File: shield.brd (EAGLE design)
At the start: 25.6 x 28 mm, 12 parts

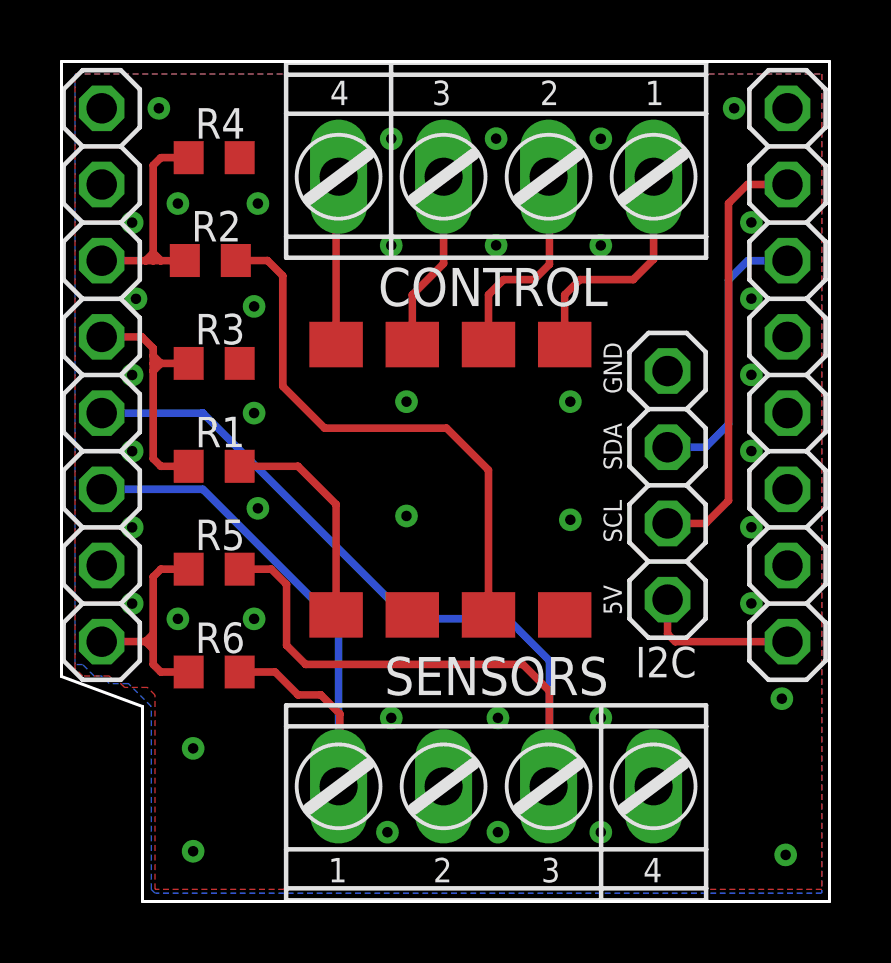
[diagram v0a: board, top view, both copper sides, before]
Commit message: Tweak layout and add lables
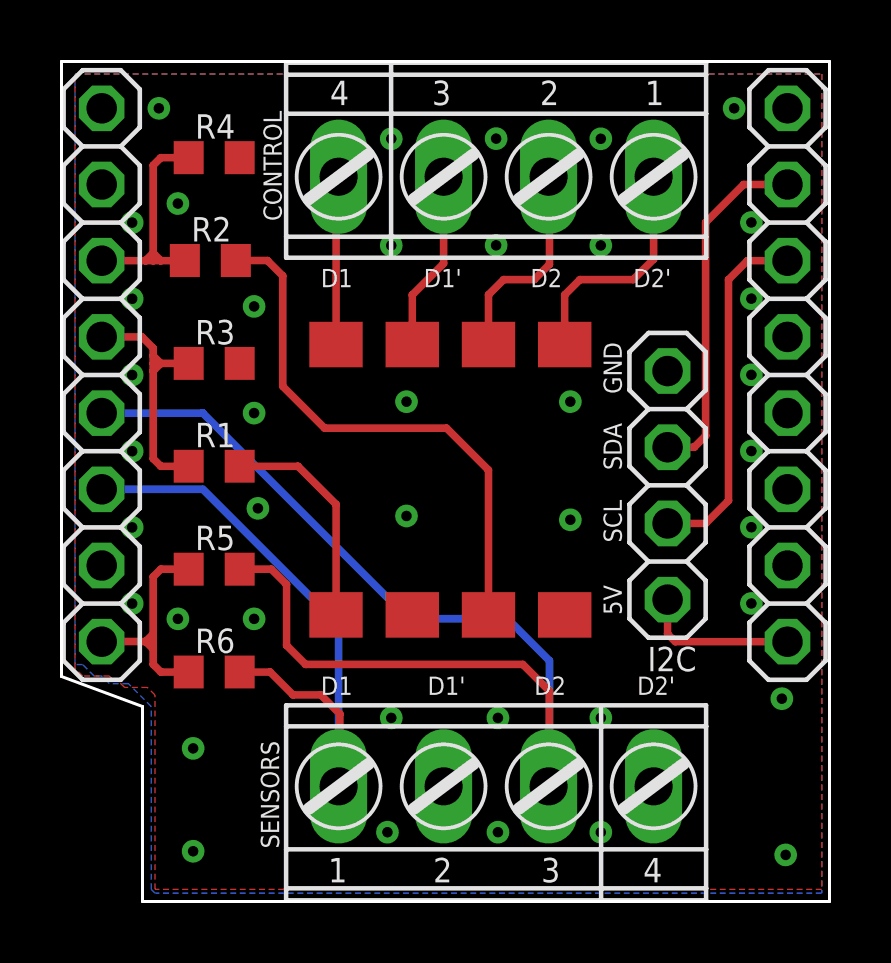
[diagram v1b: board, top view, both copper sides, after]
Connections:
- net D1: now also WEMOS_R.3; no longer WEMOS_R.2
- net D2: now also WEMOS_R.2; no longer WEMOS_R.3
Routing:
- net D1: track 14.5 -> 11.9 mm
- net D2: track 9.40 -> 11.8 mm
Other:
- board text added: "D1"
- board text added: "D1'"
- board text added: "D2"
- board text added: "D2'"

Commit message: tweak silkscreen and add some missing files
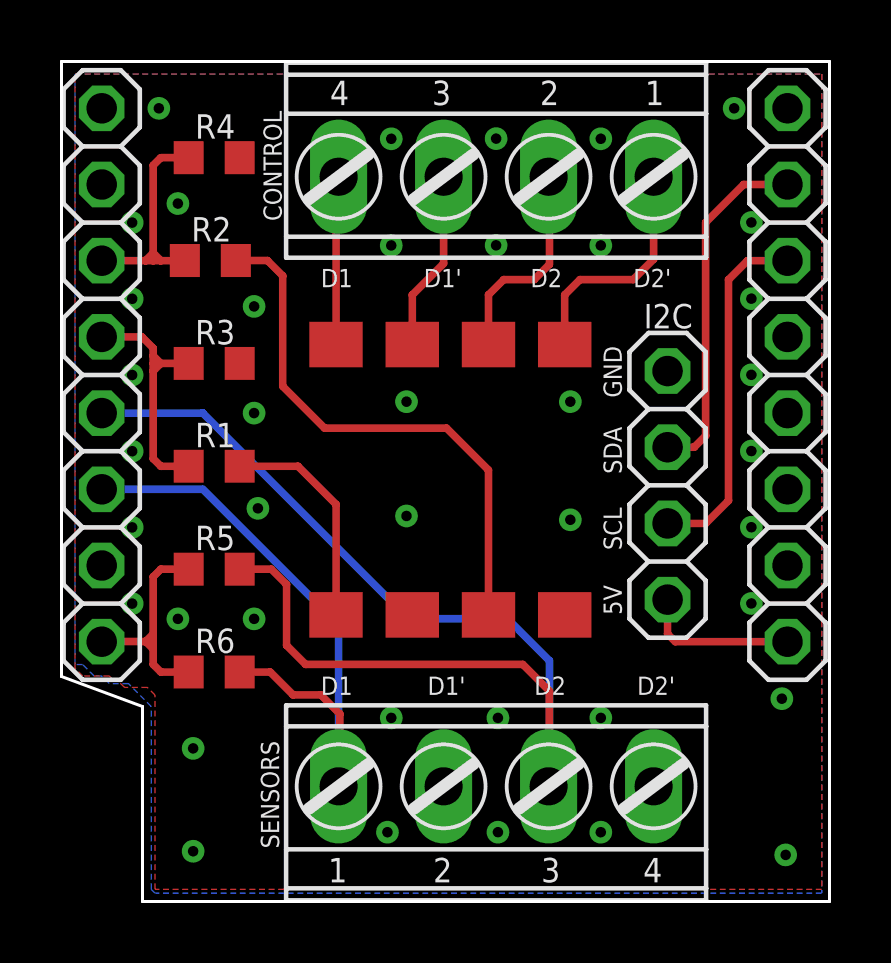
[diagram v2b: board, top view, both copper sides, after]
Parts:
- CONTROL, SENSORS: device con-ptr500:AK550/4 -> shield:AK550/4
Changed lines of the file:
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@@
 <grid distance="5" unitdist="mil" unit="mil" style="lines" multiple="1" display="yes" altdistance="5" altunitdist="mil" altunit="mil"/>
 <layers>
-<layer number="1" name="Top" color="4" fill="1" visible="yes" active="yes"/>
-<layer number="16" name="Bottom" color="1" fill="1" visible="no" active="yes"/>
+<layer number="1" name="Top" color="4" fill="1" visible="no" active="yes"/>
+<layer number="16" name="Bottom" color="1" fill="1" visible="yes" active="yes"/>
 <layer number="17" name="Pads" color="2" fill="1" visible="yes" active="yes"/>
 <layer number="18" name="Vias" color="2" fill="1" visible="yes" active="yes"/>
 <layer number="19" name="Unrouted" color="6" fill="1" visible="yes" active="yes"/>
 <layer number="20" name="Dimension" color="24" fill="1" visible="yes" active="yes"/>
-<layer number="21" name="tPlace" color="7" fill="1" visible="yes" active="yes"/>
-<layer number="22" name="bPlace" color="7" fill="1" visible="no" active="yes"/>
-<layer number="23" name="tOrigins" color="15" fill="1" visible="yes" active="yes"/>
-<layer number="24" name="bOrigins" color="15" fill="1" visible="no" active="yes"/>
-<layer number="25" name="tNames" color="7" fill="1" visible="yes" active="yes"/>
-<layer number="26" name="bNames" color="7" fill="1" visible="no" active="yes"/>
+<layer number="21" name="tPlace" color="7" fill="1" visible="no" active="yes"/>
+<layer number="22" name="bPlace" color="7" fill="1" visible="yes" active="yes"/>
+<layer number="23" name="tOrigins" color="15" fill="1" visible="no" active="yes"/>
+<layer number="24" name="bOrigins" color="15" fill="1" visible="yes" active="yes"/>
+<layer number="25" name="tNames" color="7" fill="1" visible="no" active="yes"/>
+<layer number="26" name="bNames" color="7" fill="1" visible="yes" active="yes"/>
 <layer number="27" name="tValues" color="7" fill="1" visible="no" active="yes"/>
 <layer number="28" name="bValues" color="7" fill="1" visible="no" active="yes"/>
@@
 <layer number="37" name="tTest" color="7" fill="1" visible="no" active="yes"/>
 <layer number="38" name="bTest" color="7" fill="1" visible="no" active="yes"/>
-<layer number="39" name="tKeepout" color="4" fill="11" visible="yes" active="yes"/>
-<layer number="40" name="bKeepout" color="1" fill="11" visible="no" active="yes"/>
-<layer number="41" name="tRestrict" color="4" fill="10" visible="yes" active="yes"/>
-<layer number="42" name="bRestrict" color="1" fill="10" visible="no" active="yes"/>
+<layer number="39" name="tKeepout" color="4" fill="11" visible="no" active="yes"/>
+<layer number="40" name="bKeepout" color="1" fill="11" visible="yes" active="yes"/>
+<layer number="41" name="tRestrict" color="4" fill="10" visible="no" active="yes"/>
+<layer number="42" name="bRestrict" color="1" fill="10" visible="yes" active="yes"/>
 <layer number="43" name="vRestrict" color="2" fill="10" visible="no" active="yes"/>
 <layer number="44" name="Drills" color="7" fill="1" visible="no" active="yes"/>
@@
 <layer number="49" name="Reference" color="7" fill="1" visible="no" active="yes"/>
 <layer number="50" name="dxf" color="7" fill="1" visible="no" active="no"/>
-<layer number="51" name="tDocu" color="7" fill="1" visible="yes" active="yes"/>
-<layer number="52" name="bDocu" color="7" fill="1" visible="no" active="yes"/>
+<layer number="51" name="tDocu" color="7" fill="1" visible="no" active="yes"/>
+<layer number="52" name="bDocu" color="7" fill="1" visible="yes" active="yes"/>
 <layer number="53" name="tGND_GNDA" color="7" fill="1" visible="no" active="no"/>
 <layer number="54" name="bGND_GNDA" color="7" fill="1" visible="no" active="no"/>
@@
 <rectangle x1="24.507190625" y1="4.3395875" x2="24.751028125" y2="4.34720625" layer="200"/>
 <text x="5.76325625" y="25.57525625" size="1.016" layer="26" font="vector" rot="MR270">Garage Door Control v1.0</text>
-<text x="18.796" y="12.065" size="0.6096" layer="25" rot="R90">SCL</text>
-<text x="18.796" y="14.478" size="0.6096" layer="25" rot="R90">SDA</text>
-<text x="18.796" y="17.018" size="0.6096" layer="25" rot="R90">GND</text>
+<text x="18.796" y="11.811" size="0.6096" layer="25" rot="R90">SCL</text>
+<text x="18.796" y="14.351" size="0.6096" layer="25" rot="R90">SDA</text>
+<text x="18.796" y="16.891" size="0.6096" layer="25" rot="R90">GND</text>
 <text x="18.796" y="9.652" size="0.6096" layer="25" rot="R90">5V</text>
 <text x="8.763" y="20.574" size="0.6096" layer="25">D1</text>
@@
 <attribute name="MPN" value="TLP206GA(F)" x="9.271" y="9.652" size="1.778" layer="27" display="off"/>
 </element>
-<element name="CONTROL" library="con-ptr500" package="AK550/4" value="Screw" x="14.605" y="24.257" smashed="yes" rot="R180">
+<element name="CONTROL" library="shield" package="AK550/4" value="Screw" x="14.605" y="24.257" smashed="yes" rot="R180">
 <attribute name="NAME" x="6.851" y="26.4554" size="0.6096" layer="25" ratio="10" rot="R270"/>
 <attribute name="VALUE" x="21.8544" y="30.397" size="1.778" layer="27" ratio="10" rot="R180"/>
 </element>
-<element name="SENSORS" library="con-ptr500" package="AK550/4" value="Screw" x="14.605" y="3.937" smashed="yes">
+<element name="SENSORS" library="shield" package="AK550/4" value="Screw" x="14.605" y="3.937" smashed="yes">
 <attribute name="NAME" x="7.373" y="1.8656" size="0.6096" layer="25" ratio="10" rot="R90"/>
 <attribute name="VALUE" x="7.3556" y="-2.203" size="1.778" layer="27" ratio="10"/>
@@
 </element>
 <element name="I2C" library="pinhead_v2" package="1X04/OCT" value="Header" x="20.32" y="13.97" smashed="yes" rot="R90">
-<attribute name="NAME" x="21.2852" y="8.5852" size="0.8128" layer="25" ratio="10" rot="R180"/>
+<attribute name="NAME" x="21.1582" y="20.0152" size="0.8128" layer="25" ratio="10" rot="R180"/>
 <attribute name="VALUE" x="23.495" y="8.89" size="1.27" layer="27" rot="R90"/>
 </element>

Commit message: Changed to active low, changed chip, updated silkscreen
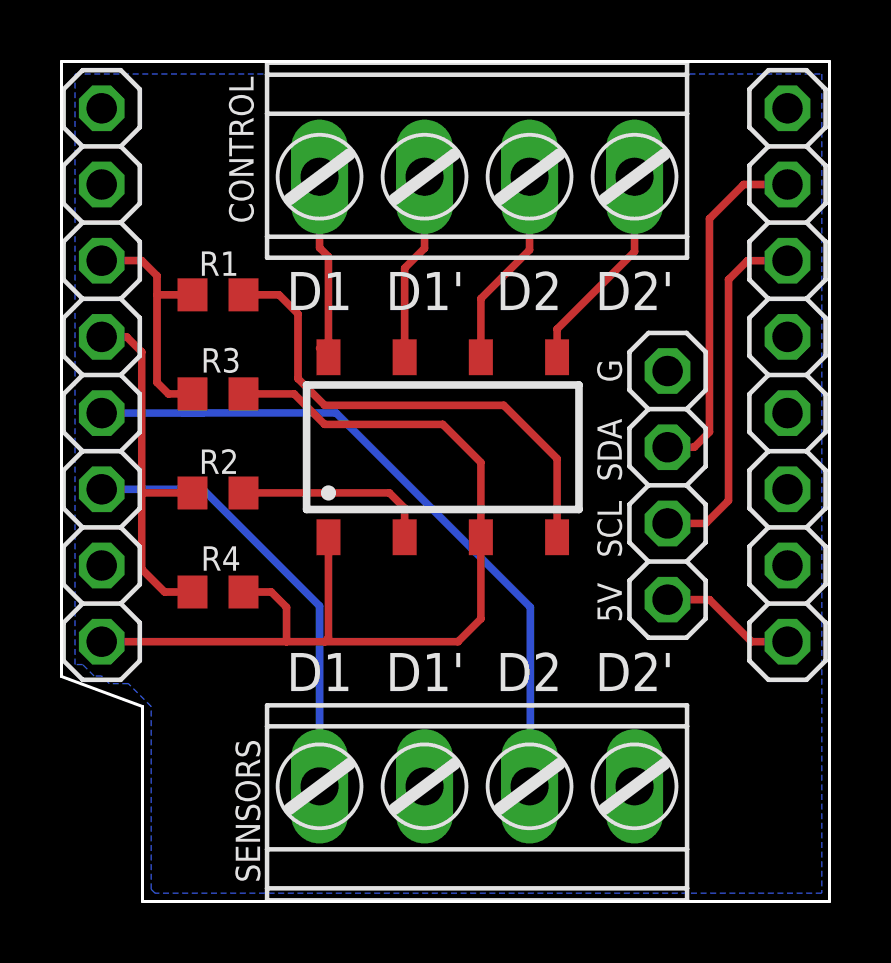
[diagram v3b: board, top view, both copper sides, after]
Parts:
- removed R5, R6: 10k, resistor:R0603
- CONTROL, SENSORS: device shield:AK550/4 -> shield:AK500/4-N
- U$1: device ICCollection:SMT8 -> shield:SOP08
- moved R4 14.5 mm to (5.33, 10.4), turned to 180 degrees
- moved R2 7.75 mm to (5.33, 13.7)
- moved U$1 6.62 mm to (12.8, 15.2)
- moved R1 5.72 mm to (5.33, 20.3)
- moved R3 1.02 mm to (5.33, 17.0), turned to 180 degrees
- moved CONTROL 0.63 mm to (14.0, 24.3)
- moved SENSORS 0.63 mm to (14.0, 3.94)
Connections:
- net 3.3V: now also R3.1, R4.1, U$1.1, U$1.3; no longer R5.1, R6.1
- net D0: now also R1.1, R3.2; no longer R2.1, R4.1
- net D5: now also R2.1, R4.2; no longer R1.1, R3.1
- net D6: no longer R5.2
- net D7: no longer R6.2
- net GND: no longer R3.2, R4.2, U$1.P$2, U$1.P$4
- net N$1: now also U$1.5; no longer U$1.P$5
- net N$2: now also U$1.7; no longer U$1.P$7
- net N$3: now also U$1.6; no longer U$1.P$6
- net N$4: now also R2.2, U$1.2; no longer R1.2, U$1.P$1
- net N$5: now also U$1.8; no longer U$1.P$8
- net N$6: now also R1.2, U$1.4; no longer R2.2, U$1.P$3
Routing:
- net 3.3V: track 7.93 -> 33.4 mm
- net D6: track 38.9 -> 23.6 mm
- net D7: track 21.5 -> 14.9 mm
- net D5: track 8.74 -> 12.5 mm
- net N$6: track 18.3 -> 16.6 mm
- net N$5: track 5.63 -> 6.56 mm
- net N$4: track 7.42 -> 6.55 mm
- net N$1: track 7.86 -> 7.09 mm
- net 5V: track 5.25 -> 4.58 mm
- removed copper zone on layer 1, net GND
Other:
- board text added: "G"
- board text added: "Garage Door Control v2.0"
- board text removed: "GND"
- board text removed: "Garage Door Control v1.0"

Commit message: Fix silkscreen for I2C, update values in schematic.
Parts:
- R1, R2: value 170 -> 220
- renumbered U$1 to TLP206GA(F)
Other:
- board text added: "Garage Door Control v2.1"
- board text removed: "Garage Door Control v2.0"
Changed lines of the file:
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@@
 <rectangle x1="24.253190625" y1="4.20496875" x2="24.497028125" y2="4.2125875" layer="200"/>
 <rectangle x1="24.253190625" y1="4.2125875" x2="24.497028125" y2="4.22020625" layer="200"/>
-<text x="3.98525625" y="25.70225625" size="1.016" layer="26" font="vector" rot="MR270">Garage Door Control v2.0</text>
-<text x="18.796" y="11.557" size="0.8128" layer="25" rot="R90">SCL</text>
-<text x="18.796" y="14.097" size="0.8128" layer="25" rot="R90">SDA</text>
+<text x="3.98525625" y="25.70225625" size="1.016" layer="26" font="vector" rot="MR270">Garage Door Control v2.1</text>
+<text x="18.796" y="14.224" size="0.8128" layer="25" rot="R90">SCL</text>
+<text x="18.796" y="11.43" size="0.8128" layer="25" rot="R90">SDA</text>
 <text x="18.796" y="17.399" size="0.8128" layer="25" rot="R90">G</text>
 <text x="18.796" y="9.398" size="0.8128" layer="25" rot="R90">5V</text>
@@
 <attribute name="VALUE" x="-1.717040625" y="27.80791875" size="1.27" layer="27" rot="R270"/>
 </element>
-<element name="U$1" library="shield" package="SOP08" value="TLP206A" x="12.827" y="15.24" smashed="yes">
+<element name="TLP206GA(F)" library="shield" package="SOP08" value="TLP206A" x="12.827" y="15.24" smashed="yes">
 <attribute name="MPN" value="TLP206GA(F)" x="12.827" y="15.24" size="1.778" layer="27" display="off"/>
 </element>
@@
 <attribute name="VALUE" x="6.7206" y="-2.203" size="1.778" layer="27" ratio="10"/>
 </element>
-<element name="R1" library="resistor" library_urn="urn:adsk.eagle:library:348" package="R0603" package3d_urn="urn:adsk.eagle:package:23555/3" value="170" x="5.334" y="20.32" smashed="yes">
+<element name="R1" library="resistor" library_urn="urn:adsk.eagle:library:348" package="R0603" package3d_urn="urn:adsk.eagle:package:23555/3" value="220" x="5.334" y="20.32" smashed="yes">
 <attribute name="NAME" x="4.699" y="20.955" size="0.8128" layer="25"/>
 <attribute name="VALUE" x="4.699" y="18.415" size="1.27" layer="27"/>
 </element>
-<element name="R2" library="resistor" library_urn="urn:adsk.eagle:library:348" package="R0603" package3d_urn="urn:adsk.eagle:package:23555/3" value="170" x="5.334" y="13.716" smashed="yes">
+<element name="R2" library="resistor" library_urn="urn:adsk.eagle:library:348" package="R0603" package3d_urn="urn:adsk.eagle:package:23555/3" value="220" x="5.334" y="13.716" smashed="yes">
 <attribute name="NAME" x="4.699" y="14.351" size="0.8128" layer="25"/>
 <attribute name="VALUE" x="4.699" y="11.811" size="1.27" layer="27"/>
@@
 <signal name="N$2">
 <contactref element="CONTROL" pad="3"/>
-<contactref element="U$1" pad="7"/>
+<contactref element="TLP206GA(F)" pad="7"/>
 <wire x1="12.22" y1="24.257" x2="12.22" y2="21.872" width="0.254" layer="1"/>
 <wire x1="12.22" y1="21.872" x2="11.557" y2="21.209" width="0.254" layer="1"/>
@@
 <signal name="N$3">
 <contactref element="CONTROL" pad="2"/>
-<contactref element="U$1" pad="6"/>
+<contactref element="TLP206GA(F)" pad="6"/>
 <wire x1="15.72" y1="24.257" x2="15.72" y2="21.816" width="0.254" layer="1"/>
 <wire x1="15.72" y1="21.816" x2="14.097" y2="20.193" width="0.254" layer="1"/>
@@
 <signal name="N$5">
 <contactref element="CONTROL" pad="4"/>
-<contactref element="U$1" pad="8"/>
+<contactref element="TLP206GA(F)" pad="8"/>
 <wire x1="9.017" y1="18.24" x2="8.72" y2="18.537" width="0.254" layer="1"/>
 <wire x1="8.72" y1="24.257" x2="8.72" y2="21.887" width="0.254" layer="1"/>
@@
 <signal name="N$1">
 <contactref element="CONTROL" pad="1"/>
-<contactref element="U$1" pad="5"/>
+<contactref element="TLP206GA(F)" pad="5"/>
 <wire x1="19.22" y1="24.257" x2="19.22" y2="21.76" width="0.254" layer="1"/>
 <wire x1="16.637" y1="19.177" x2="16.637" y2="18.24" width="0.254" layer="1"/>
@@
 <wire x1="8.89" y1="8.75791875" x2="13.335" y2="8.75791875" width="0.254" layer="1"/>
 <wire x1="7.62" y1="9.906" x2="7.62" y2="8.75791875" width="0.254" layer="1"/>
-<contactref element="U$1" pad="1"/>
-<contactref element="U$1" pad="3"/>
+<contactref element="TLP206GA(F)" pad="1"/>
+<contactref element="TLP206GA(F)" pad="3"/>
 <wire x1="9.017" y1="12.24" x2="9.017" y2="8.88491875" width="0.254" layer="1"/>
 <wire x1="9.017" y1="8.88491875" x2="8.89" y2="8.75791875" width="0.254" layer="1"/>
@@
 </signal>
 <signal name="N$4">
-<contactref element="U$1" pad="2"/>
+<contactref element="TLP206GA(F)" pad="2"/>
 <contactref element="R2" pad="2"/>
 <wire x1="6.184" y1="13.716" x2="11.049" y2="13.716" width="0.254" layer="1"/>
@@
 </signal>
 <signal name="N$6">
-<contactref element="U$1" pad="4"/>
+<contactref element="TLP206GA(F)" pad="4"/>
 <contactref element="R1" pad="2"/>
 <wire x1="6.184" y1="20.32" x2="7.366" y2="20.32" width="0.254" layer="1"/>
